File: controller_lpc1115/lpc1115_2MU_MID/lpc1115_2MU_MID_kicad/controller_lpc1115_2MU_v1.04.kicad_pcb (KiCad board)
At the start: 2 copper layers, 57.5 x 32 mm, 69 parts, among them J1 Conn_01x10, J2 Conn_UI, J3 Conn_JTAG, Q1 FZT753, Q2 BC847, Q3 BC856, SW1 SW_Omron_B3FS, U1 LPC1115FBD48-303, U2 TPS560430, X1 12MHz

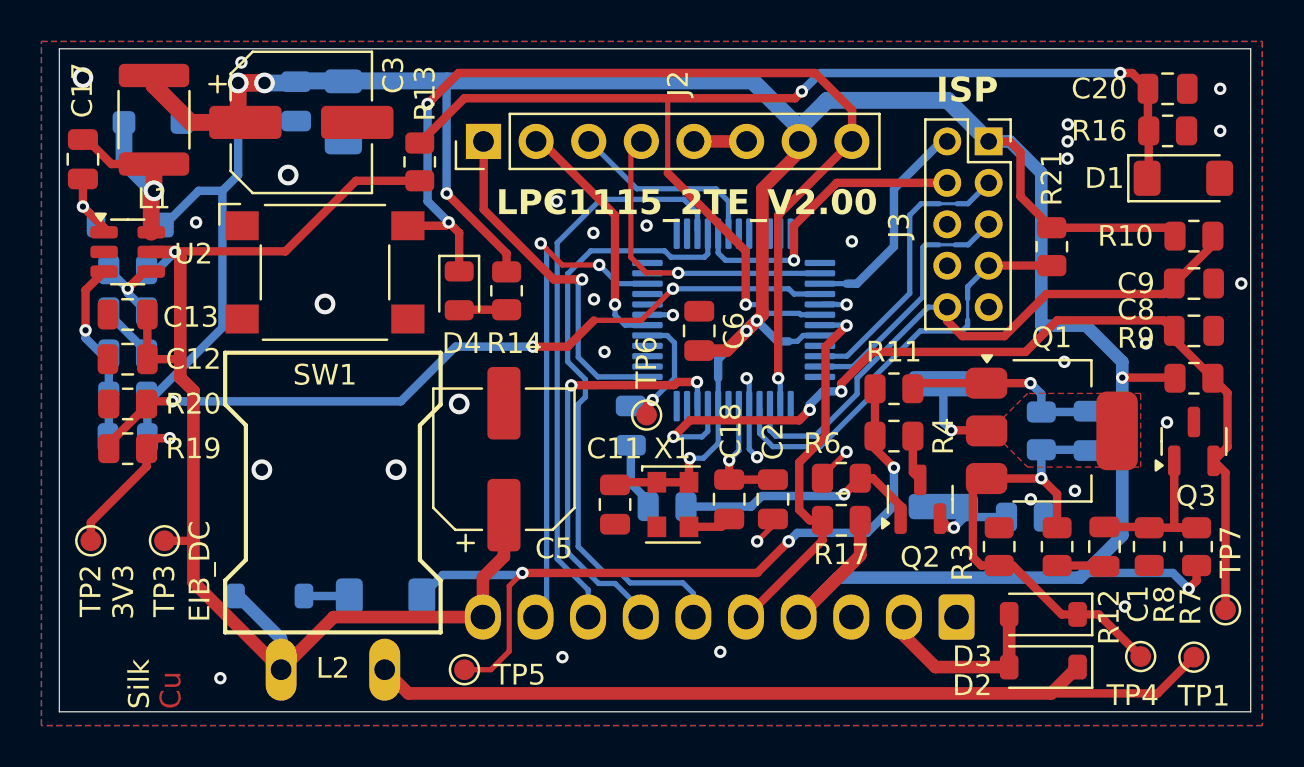
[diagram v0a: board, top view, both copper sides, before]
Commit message: fixups for 2MU/4MU controllers - use Seiko oszillator
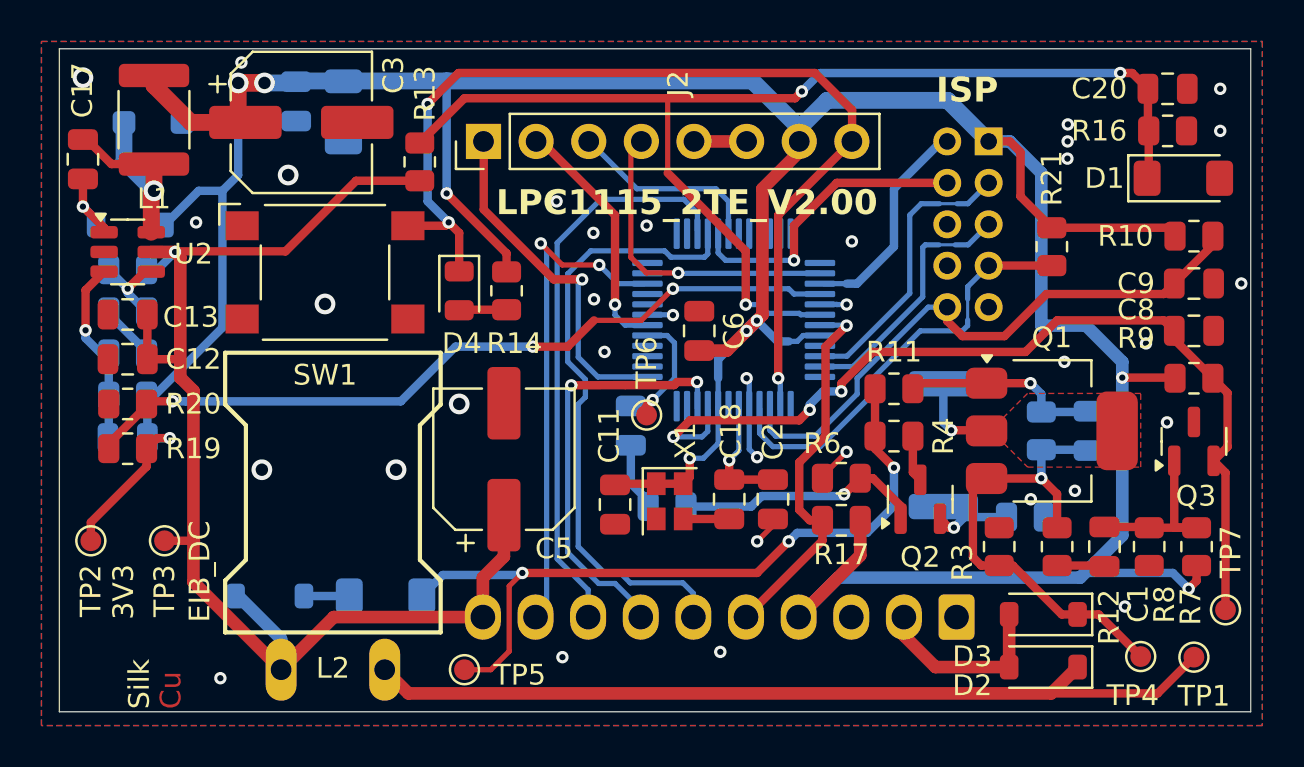
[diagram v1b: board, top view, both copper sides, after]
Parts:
- J3: footprint Connector_PinSocket_2.00mm:PinSocket_2x05_P2.00mm_Vertical -> Connector_PinHeader_2.00mm:PinHeader_2x05_P2.00mm_Vertical; moved to B.Cu
- X1: footprint Oscillator:Oscillator_SMD_EuroQuartz_XO32-4Pin_3.2x2.5mm -> Oscillator:Oscillator_SMD_SeikoEpson_SG210-4Pin_2.5x2.0mm
- moved X1 0.22 mm to (154.4, 106.2), turned to -90 degrees
- turned J3 to 180 degrees

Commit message: finally standardize selected parts on all boards
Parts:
- C12: value 4.7µ/35V -> 4.7u/35V
- C15: value 47µ/10V -> 47u/10V
- C3: value 100µ/10V -> 100u/10V
- C5: value 100µ/35V -> 100u/35V
- D10: value 7,5V -> 7V5
- D5: footprint Diode_SMD:D_SOD-123F -> Diode_SMD:D_SOD-123
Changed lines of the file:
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@@
 			)
 		)
-		(property "Value" "100µ/35V"
+		(property "Value" "100u/35V"
 			(at 0 4.35 -90)
 			(layer "F.Fab")
@@
 			)
 		)
-		(property "Value" "4.7µ/35V"
+		(property "Value" "4.7u/35V"
 			(at 0 1.68 0)
 			(layer "F.Fab")
@@
 				(font
 					(size 1.27 1.27)
+					(thickness 0.15)
 				)
 			)
@@
 				(font
 					(size 1.27 1.27)
+					(thickness 0.15)
 				)
 			)
@@
 				(font
 					(size 1.27 1.27)
+					(thickness 0.15)
 				)
 			)
@@
 			)
 		)
-		(property "Value" "100µ/10V"
+		(property "Value" "100u/10V"
 			(at 0 4.35 0)
 			(layer "F.Fab")
@@
 				(font
 					(size 1.27 1.27)
+					(thickness 0.15)
 				)
 				(justify mirror)
@@
 				(font
 					(size 1.27 1.27)
+					(thickness 0.15)
 				)
 				(justify mirror)
@@
 				(font
 					(size 1.27 1.27)
+					(thickness 0.15)
 				)
 				(justify mirror)
@@
 			)
 		)
-		(property "Value" "7,5V"
+		(property "Value" "7V5"
 			(at 0 -2 0)
 			(layer "B.Fab")
@@
 			)
 		)
-		(property "Value" "47µ/10V"
+		(property "Value" "47u/10V"
 			(at 0 -1.85 -90)
 			(layer "B.Fab")
@@
 		(sheetname "Stammblatt")
 		(sheetfile "controller_lpc1115_2MU_v1.04.kicad_sch")
-		(attr smd dnp)
+		(attr smd exclude_from_bom dnp)
 		(fp_line
 			(start -2.36 -1)
@@
 		)
 	)
-	(footprint "Diode_SMD:D_SOD-123F"
+	(footprint "Diode_SMD:D_SOD-123"
 		(layer "B.Cu")
 		(at 129.4928 87.8876)
-		(descr "D_SOD-123F")
-		(tags "D_SOD-123F")
+		(descr "SOD-123")
+		(tags "SOD-123")
 		(property "Reference" "D5"
-			(at -0.0508 1.9304 0)
+			(at 0 2 180)
 			(layer "B.SilkS")
 			(effects
@@
 		)
 		(property "Value" "RB060M-60 / MBR 140SFT1G"
-			(at 0 -2.1 0)
+			(at 0 -2.1 180)
 			(layer "B.Fab")
 			(effects
@@
 			)
 		)
-		(property "Footprint" "Diode_SMD:D_SOD-123F"
+		(property "Footprint" "Diode_SMD:D_SOD-123"
 			(at 0 0 180)
 			(unlocked yes)
@@
 		(attr smd)
 		(fp_line
-			(start -2.21 -1)
-			(end -2.21 1)
+			(start -2.36 -1)
+			(end -2.36 1)
 			(stroke
 				(width 0.12)
@@
 		(fp_line
 			(start 1.65 -1)
-			(end -2.21 -1)
+			(end -2.36 -1)
 			(stroke
 				(width 0.12)
@@
 		(fp_line
 			(start 1.65 1)
-			(end -2.21 1)
+			(end -2.36 1)
 			(stroke
 				(width 0.12)
@@
 		)
 		(fp_line
-			(start -2.2 -1.15)
-			(end -2.2 1.15)
+			(start -2.35 -1.15)
+			(end -2.35 1.15)
 			(stroke
 				(width 0.05)
@@
 		)
 		(fp_line
-			(start -2.2 -1.15)
-			(end 2.2 -1.15)
+			(start -2.35 -1.15)
+			(end 2.35 -1.15)
 			(stroke
 				(width 0.05)
@@
 		)
 		(fp_line
-			(start 2.2 -1.15)
-			(end 2.2 1.15)
+			(start 2.35 -1.15)
+			(end 2.35 1.15)
 			(stroke
 				(width 0.05)
@@
 		)
 		(fp_line
-			(start 2.2 1.15)
-			(end -2.2 1.15)
+			(start 2.35 1.15)
+			(end -2.35 1.15)
 			(stroke
 				(width 0.05)
@@
 		)
 		(fp_text user "${REFERENCE}"
-			(at -0.127 1.905 0)
+			(at 0 2 180)
 			(layer "B.Fab")
 			(effects
@@
 		)
 		(pad "1" smd roundrect
-			(at -1.4 0)
-			(size 1.1 1.1)
+			(at -1.65 0)
+			(size 0.9 1.2)
 			(layers "B.Cu" "B.Paste" "B.Mask")
-			(roundrect_rratio 0.2272727273)
+			(roundrect_rratio 0.25)
 			(net 64 "Net-(D5-K)")
 			(pinfunction "K")
@@
 		)
 		(pad "2" smd roundrect
-			(at 1.4 0)
-			(size 1.1 1.1)
+			(at 1.65 0)
+			(size 0.9 1.2)
 			(layers "B.Cu" "B.Paste" "B.Mask")
-			(roundrect_rratio 0.2272727273)
+			(roundrect_rratio 0.25)
 			(net 1 "GND")
 			(pinfunction "A")
 			(pintype "passive")
 		)
-		(model "${KICAD8_3DMODEL_DIR}/Diode_SMD.3dshapes/D_SOD-123F.wrl"
+		(model "${KICAD8_3DMODEL_DIR}/Diode_SMD.3dshapes/D_SOD-123.wrl"
 			(offset
 				(xyz 0 0 0)
@@
 		(sheetname "Stammblatt")
 		(sheetfile "controller_lpc1115_2MU_v1.04.kicad_sch")
-		(attr smd dnp)
+		(attr smd exclude_from_bom dnp)
 		(fp_line
 			(start 0.261252 -0.735)
@@
 	)
 	(segment
-		(start 128.0928 89.7388)
-		(end 128.0928 87.8876)
+		(start 129.54 91.186)
+		(end 127.8428 89.4888)
 		(width 0.8128)
 		(layer "B.Cu")
@@
 	)
 	(segment
-		(start 129.54 91.186)
-		(end 128.0928 89.7388)
+		(start 127.8428 89.4888)
+		(end 127.8428 87.8876)
 		(width 0.8128)
 		(layer "B.Cu")

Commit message: final for manufacturing
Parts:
- R13: value 91k -> 43k; moved to B.Cu
- R16: value 10k -> 6k2
- moved R13 18.8 mm to (140.0, 108.5), turned to 0 degrees
- moved D10 5.59 mm to (135.1, 110.7)
- moved D6 5.33 mm to (140.5, 110.7)
- moved D4 0.25 mm to (144.0, 96.0)
- moved R14 0.25 mm to (146.3, 96.0)
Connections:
- D10 pad 1: Net-(D10-K) -> /EIB_DC
- D6 pad 1: Net-(D10-K) -> Net-(D6-K)
- D6 pad 2: /EIB_DC -> Net-(D10-A)
- R11 pad 2: Net-(D10-A) -> Net-(D6-K)
- R13 pad 1: /EIB_DC -> Net-(D10-A)
- R4 pad 2: Net-(D10-A) -> Net-(D6-K)
- TP5 pad 1: Net-(D10-A) -> Net-(D6-K)
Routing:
- net Net-(D6-K): track 0.00 -> 37.6 mm, vias 0 -> 3
- net Net-(D10-A): track 37.2 -> 4.32 mm, vias 3 -> 0
- net /BUS_V: track 56.5 -> 60.2 mm, vias 3 -> 4
- net Net-(D10-K): track 2.19 -> 0.00 mm
- net +3V3: track 186.1 -> 186.7 mm
- net GND: vias 35 -> 36

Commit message: update controller_lpc1115_2MU_v1.04
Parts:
- C17: value 15n -> 100n
- R22: value 88k7 -> 51k
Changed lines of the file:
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@@
 		(sheetname "Stammblatt")
 		(sheetfile "controller_lpc1115_2MU_v1.04.kicad_sch")
-		(attr exclude_from_pos_files)
+		(attr exclude_from_pos_files exclude_from_bom)
 		(fp_circle
 			(center 0 0)
@@
 		(sheetname "Stammblatt")
 		(sheetfile "controller_lpc1115_2MU_v1.04.kicad_sch")
-		(attr exclude_from_pos_files)
+		(attr exclude_from_pos_files exclude_from_bom)
 		(fp_circle
 			(center 0 0)
@@
 		(sheetname "Stammblatt")
 		(sheetfile "controller_lpc1115_2MU_v1.04.kicad_sch")
-		(attr exclude_from_pos_files)
+		(attr exclude_from_pos_files exclude_from_bom)
 		(fp_circle
 			(center 0 0)
@@
 		(sheetname "Stammblatt")
 		(sheetfile "controller_lpc1115_2MU_v1.04.kicad_sch")
-		(attr exclude_from_pos_files)
+		(attr exclude_from_pos_files exclude_from_bom)
 		(fp_circle
 			(center 0 0)
@@
 		(sheetname "Stammblatt")
 		(sheetfile "controller_lpc1115_2MU_v1.04.kicad_sch")
-		(attr exclude_from_pos_files)
+		(attr exclude_from_pos_files exclude_from_bom)
 		(fp_circle
 			(center 0 0)
@@
 			)
 		)
-		(property "Value" "15n"
+		(property "Value" "100n"
 			(at 0 1.68 90)
 			(layer "F.Fab")
@@
 		(sheetname "Stammblatt")
 		(sheetfile "controller_lpc1115_2MU_v1.04.kicad_sch")
-		(attr exclude_from_pos_files)
+		(attr exclude_from_pos_files exclude_from_bom)
 		(fp_circle
 			(center 0 0)
@@
 		(sheetname "Stammblatt")
 		(sheetfile "controller_lpc1115_2MU_v1.04.kicad_sch")
-		(attr exclude_from_pos_files)
+		(attr exclude_from_pos_files exclude_from_bom)
 		(fp_circle
 			(center 0 0)
@@
 		(tags "resistor")
 		(property "Reference" "R13"
-			(at 0 -1.524 360)
+			(at 0 -1.524 0)
 			(layer "B.SilkS")
 			(effects
@@
 		)
 		(property "Value" "43k"
-			(at 0 -1.65 360)
+			(at 0 -1.65 0)
 			(layer "B.Fab")
 			(effects
@@
 		)
 		(fp_text user "${REFERENCE}"
-			(at 0 0 360)
+			(at 0 0 0)
 			(layer "B.Fab")
 			(effects
@@
 			)
 		)
-		(property "Value" "88k7"
+		(property "Value" "51k"
 			(at 0 -1.65 0)
 			(layer "B.Fab")

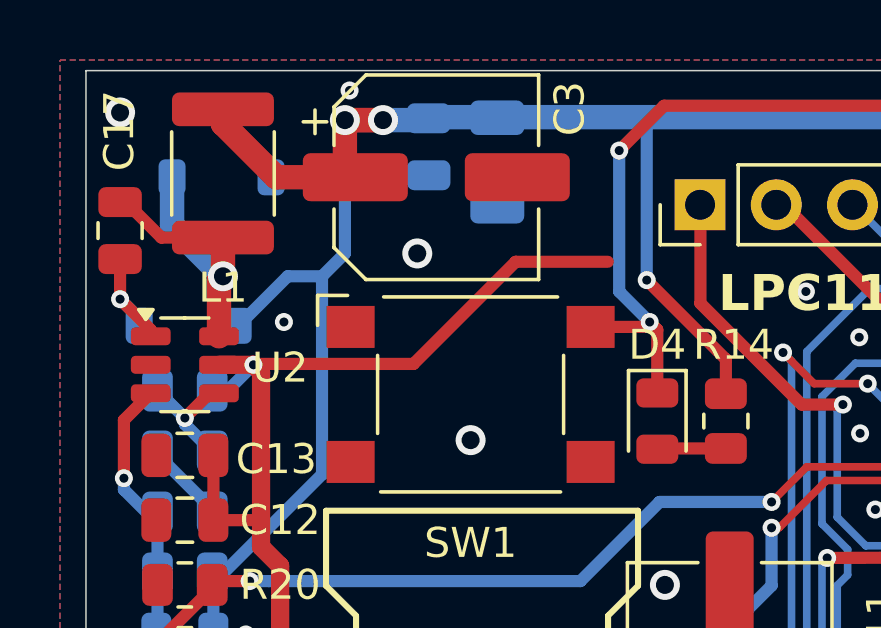
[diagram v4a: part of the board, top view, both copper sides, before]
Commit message: update xtal caps, eib_in cap+resistor, bus_v resistors
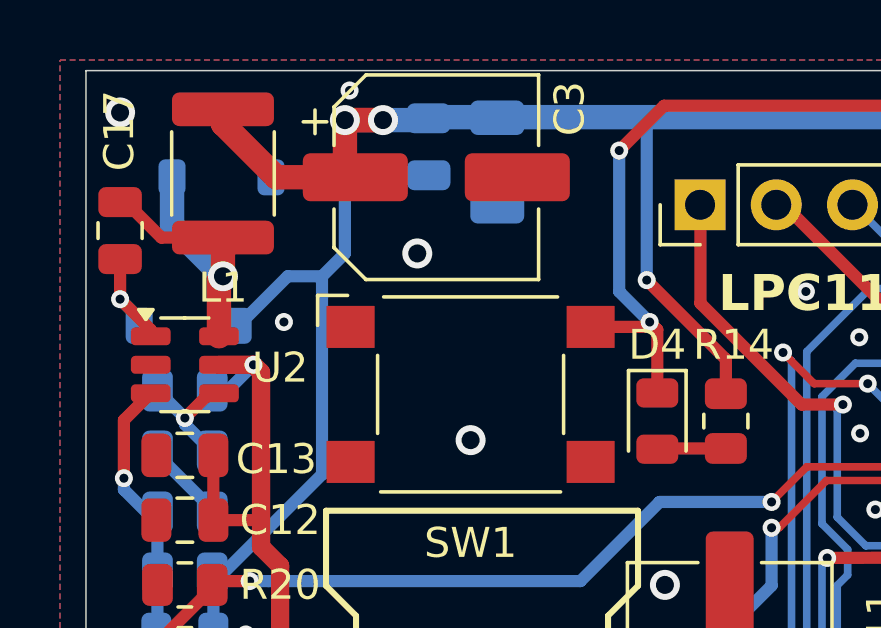
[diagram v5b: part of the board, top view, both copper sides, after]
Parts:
- C18: value 100p -> 22p
- C2: value 220p -> 22p
- R8: value 47k -> 100k
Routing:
- net /EIB_DC: track 64.4 -> 51.2 mm
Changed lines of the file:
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@@
 			)
 		)
-		(property "Value" "220p"
+		(property "Value" "22p"
 			(at 0 1.68 -90)
 			(layer "F.Fab")
@@
 			)
 		)
-		(property "Value" "47k"
+		(property "Value" "100k"
 			(at 0 1.65 90)
 			(layer "F.Fab")
@@
 			)
 		)
-		(property "Value" "100p"
+		(property "Value" "22p"
 			(at 0 1.68 -90)
 			(layer "F.Fab")
@@
 		(sheetname "Stammblatt")
 		(sheetfile "controller_lpc1115_2MU_v1.04.kicad_sch")
-		(attr smd)
+		(attr smd exclude_from_bom dnp)
 		(fp_line
 			(start -0.227064 -0.735)
@@
 		(sheetname "Stammblatt")
 		(sheetfile "controller_lpc1115_2MU_v1.04.kicad_sch")
-		(attr smd)
+		(attr smd exclude_from_bom dnp)
 		(fp_line
 			(start 0.227064 -0.735)
@@
 	)
 	(segment
-		(start 130.585 94.107)
-		(end 135.89 94.107)
-		(width 0.4064)
-		(layer "F.Cu")
-		(net 7)
-	)
-	(segment
-		(start 130.556 94.136)
-		(end 130.585 94.107)
-		(width 0.4064)
-		(layer "F.Cu")
-		(net 7)
-	)
-	(segment
 		(start 131.445 110.069)
 		(end 135.676 114.3)
@@
 	)
 	(segment
-		(start 135.89 94.107)
-		(end 139.2955 90.7015)
-		(width 0.4064)
-		(layer "F.Cu")
-		(net 7)
-	)
-	(segment
 		(start 130.81 94.39)
 		(end 130.81 100.203)
@@
 		(layer "F.Cu")
 		(net 7)
-	)
-	(segment
-		(start 139.2955 90.7015)
-		(end 142.367 90.7015)
-		(width 0.4064)
-		(layer "F.Cu")
-		(net 7)
